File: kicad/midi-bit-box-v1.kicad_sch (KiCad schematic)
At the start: 60 parts, among them IC1 LM386, IC2 DIP14, K1 TQ2-L-5V, Q1 2N3904, Q2 2N3906, Q3 2N3904, Q4 2N3904, U1 AY-3-8910, U2 L78L09_TO92, U3 NE555P

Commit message: added trimpot to control output volume
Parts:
- added LEVEL1: 100k, midi-bit-box-v1:TRIM1, symbol midi-bit-box-v1-eagle-import:TRIMMER
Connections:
- net GND: now also LEVEL1.1
- net at OUTPUT1.T: now also LEVEL1.2; no longer K1.8
- new net: K1.8, LEVEL1.3
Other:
- moved on the sheet: OUTPUT1
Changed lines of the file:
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@@
+    (stroke (width 0) (type default) (color 0 0 0 0))
+  )
+  (wire (pts (xy 373.126 162.052) (xy 373.126 165.862))
     (stroke (width 0) (type default) (color 0 0 0 0))
   )
@@
     (stroke (width 0) (type default) (color 0 0 0 0))
   )
-  (wire (pts (xy 321.31 167.64) (xy 391.668 167.64))
-    (stroke (width 0) (type default) (color 0 0 0 0))
-  )
   (wire (pts (xy 424.18 97.79) (xy 414.02 97.79))
     (stroke (width 0) (type default) (color 0 0 0 0))
   )
+  (wire (pts (xy 321.31 167.64) (xy 345.948 167.64))
+    (stroke (width 0) (type default) (color 0 0 0 0))
+  )
   (wire (pts (xy 121.92 55.88) (xy 121.92 76.2))
     (stroke (width 0) (type default) (color 0 0 0 0))
@@
     (stroke (width 0) (type default) (color 0 0 0 0))
   )
+  (wire (pts (xy 345.948 162.052) (xy 356.362 162.052))
+    (stroke (width 0) (type default) (color 0 0 0 0))
+  )
   (wire (pts (xy 331.978 242.316) (xy 344.678 242.316))
     (stroke (width 0) (type default) (color 0 0 0 0))
@@
     (stroke (width 0) (type default) (color 0 0 0 0))
   )
+  (wire (pts (xy 385.826 157.734) (xy 385.826 159.766))
+    (stroke (width 0) (type default) (color 0 0 0 0))
+  )
   (wire (pts (xy 162.56 25.4) (xy 162.56 27.94))
     (stroke (width 0) (type default) (color 0 0 0 0))
@@
     (stroke (width 0) (type default) (color 0 0 0 0))
   )
-  (wire (pts (xy 391.668 164.846) (xy 391.668 167.64))
-    (stroke (width 0) (type default) (color 0 0 0 0))
-  )
   (wire (pts (xy 240.03 17.78) (xy 224.79 17.78))
     (stroke (width 0) (type default) (color 0 0 0 0))
@@
     (stroke (width 0) (type default) (color 0 0 0 0))
   )
-  (wire (pts (xy 397.51 162.306) (xy 386.08 162.306))
+  (wire (pts (xy 396.748 155.194) (xy 385.318 155.194))
     (stroke (width 0) (type default) (color 0 0 0 0))
   )
@@
     (stroke (width 0) (type default) (color 0 0 0 0))
   )
+  (wire (pts (xy 396.748 157.734) (xy 385.826 157.734))
+    (stroke (width 0) (type default) (color 0 0 0 0))
+  )
   (wire (pts (xy 294.64 172.72) (xy 294.64 187.96))
     (stroke (width 0) (type default) (color 0 0 0 0))
@@
     (stroke (width 0) (type default) (color 0 0 0 0))
   )
+  (wire (pts (xy 369.062 162.052) (xy 373.126 162.052))
+    (stroke (width 0) (type default) (color 0 0 0 0))
+  )
   (wire (pts (xy 212.09 81.28) (xy 220.98 81.28))
     (stroke (width 0) (type default) (color 0 0 0 0))
@@
     (stroke (width 0) (type default) (color 0 0 0 0))
   )
+  (wire (pts (xy 371.348 159.766) (xy 371.348 153.416))
+    (stroke (width 0) (type default) (color 0 0 0 0))
+  )
   (wire (pts (xy 57.15 50.8) (xy 68.58 50.8))
     (stroke (width 0) (type default) (color 0 0 0 0))
@@
     (stroke (width 0) (type default) (color 0 0 0 0))
   )
+  (wire (pts (xy 373.126 165.862) (xy 378.206 165.862))
+    (stroke (width 0) (type default) (color 0 0 0 0))
+  )
   (wire (pts (xy 441.96 115.57) (xy 441.96 109.22))
     (stroke (width 0) (type default) (color 0 0 0 0))
   )
-  (wire (pts (xy 397.51 164.846) (xy 391.668 164.846))
-    (stroke (width 0) (type default) (color 0 0 0 0))
-  )
   (wire (pts (xy 196.85 149.86) (xy 172.72 149.86))
     (stroke (width 0) (type default) (color 0 0 0 0))
@@
     (stroke (width 0) (type default) (color 0 0 0 0))
   )
+  (wire (pts (xy 378.206 165.862) (xy 378.206 168.656))
+    (stroke (width 0) (type default) (color 0 0 0 0))
+  )
   (wire (pts (xy 281.94 182.88) (xy 281.94 187.96))
     (stroke (width 0) (type default) (color 0 0 0 0))
@@
     (stroke (width 0) (type default) (color 0 0 0 0))
   )
+  (wire (pts (xy 385.826 159.766) (xy 371.348 159.766))
+    (stroke (width 0) (type default) (color 0 0 0 0))
+  )
   (wire (pts (xy 434.34 97.79) (xy 441.96 97.79))
     (stroke (width 0) (type default) (color 0 0 0 0))
@@
     (stroke (width 0) (type default) (color 0 0 0 0))
   )
+  (wire (pts (xy 362.712 153.416) (xy 362.712 156.972))
+    (stroke (width 0) (type default) (color 0 0 0 0))
+  )
   (wire (pts (xy 375.666 239.776) (xy 382.778 239.776))
     (stroke (width 0) (type default) (color 0 0 0 0))
@@
     (stroke (width 0) (type default) (color 0 0 0 0))
   )
+  (wire (pts (xy 345.948 167.64) (xy 345.948 162.052))
+    (stroke (width 0) (type default) (color 0 0 0 0))
+  )
   (wire (pts (xy 132.08 93.98) (xy 144.78 93.98))
     (stroke (width 0) (type default) (color 0 0 0 0))
@@
   )
   (wire (pts (xy 396.24 13.97) (xy 388.62 13.97))
+    (stroke (width 0) (type default) (color 0 0 0 0))
+  )
+  (wire (pts (xy 371.348 153.416) (xy 362.712 153.416))
     (stroke (width 0) (type default) (color 0 0 0 0))
   )
@@
     (pin "1")
   )
-  (symbol (lib_id "Connector:AudioJack2") (at 402.59 164.846 0) (mirror y) (unit 1)
+  (symbol (lib_id "Connector:AudioJack2") (at 401.828 157.734 0) (mirror y) (unit 1)
     (in_bom yes) (on_board yes) (fields_autoplaced)
-    (property "Reference" "OUTPUT1" (id 0) (at 407.67 162.9409 0)
+    (property "Reference" "OUTPUT1" (id 0) (at 406.908 155.8289 0)
       (effects (font (size 1.27 1.27)) (justify right))
     )
-    (property "Value" "Audio Jack" (id 1) (at 407.67 165.4809 0)
+    (property "Value" "Audio Jack" (id 1) (at 406.908 158.3689 0)
       (effects (font (size 1.27 1.27)) (justify right))
     )
-    (property "Footprint" "midi-bit-box-v1:2PADS" (id 2) (at 402.59 164.846 0)
-      (effects (font (size 1.27 1.27)) hide)
-    )
-    (property "Datasheet" "~" (id 3) (at 402.59 164.846 0)
+    (property "Footprint" "midi-bit-box-v1:2PADS" (id 2) (at 401.828 157.734 0)
+      (effects (font (size 1.27 1.27)) hide)
+    )
+    (property "Datasheet" "~" (id 3) (at 401.828 157.734 0)
       (effects (font (size 1.27 1.27)) hide)
     )
@@
     (property "Datasheet" "https://www.onsemi.com/pub/Collateral/2N3903-D.PDF" (id 3) (at 365.76 187.96 0)
       (effects (font (size 1.27 1.27)) (justify left) hide)
+    )
+    (pin "1")
+    (pin "2")
+    (pin "3")
+  )
+  (symbol (lib_id "midi-bit-box-v1-eagle-import:TRIMMER") (at 362.712 162.052 90) (unit 1)
+    (in_bom yes) (on_board yes)
+    (property "Reference" "LEVEL1" (id 0) (at 362.712 164.211 90)
+      (effects (font (size 1.778 1.5113)))
+    )
+    (property "Value" "100k" (id 1) (at 362.712 166.497 90)
+      (effects (font (size 1.778 1.5113)))
+    )
+    (property "Footprint" "midi-bit-box-v1:TRIM1" (id 2) (at 362.712 162.052 0)
+      (effects (font (size 1.27 1.27)) hide)
+    )
+    (property "Datasheet" "" (id 3) (at 362.712 162.052 0)
+      (effects (font (size 1.27 1.27)) hide)
     )
     (pin "1")
@@
     (pin "2")
   )
-  (symbol (lib_id "midi-bit-box-v1-eagle-import:GND") (at 383.54 162.306 270) (unit 1)
-    (in_bom yes) (on_board yes)
-    (property "Reference" "#GND028" (id 0) (at 383.54 162.306 0)
-      (effects (font (size 1.27 1.27)) hide)
-    )
-    (property "Value" "GND" (id 1) (at 380.365 160.401 0)
-      (effects (font (size 1.778 1.5113)) (justify left bottom))
-    )
-    (property "Footprint" "midi-bit-box-v1:" (id 2) (at 383.54 162.306 0)
-      (effects (font (size 1.27 1.27)) hide)
-    )
-    (property "Datasheet" "" (id 3) (at 383.54 162.306 0)
+  (symbol (lib_id "midi-bit-box-v1-eagle-import:GND") (at 382.778 155.194 270) (unit 1)
+    (in_bom yes) (on_board yes)
+    (property "Reference" "#GND028" (id 0) (at 382.778 155.194 0)
+      (effects (font (size 1.27 1.27)) hide)
+    )
+    (property "Value" "GND" (id 1) (at 379.603 153.289 0)
+      (effects (font (size 1.778 1.5113)) (justify left bottom))
+    )
+    (property "Footprint" "midi-bit-box-v1:" (id 2) (at 382.778 155.194 0)
+      (effects (font (size 1.27 1.27)) hide)
+    )
+    (property "Datasheet" "" (id 3) (at 382.778 155.194 0)
       (effects (font (size 1.27 1.27)) hide)
     )
@@
     )
     (property "Datasheet" "" (id 3) (at 397.51 267.97 0)
+      (effects (font (size 1.27 1.27)) hide)
+    )
+    (pin "1")
+  )
+  (symbol (lib_id "midi-bit-box-v1-eagle-import:GND") (at 378.206 171.196 0) (unit 1)
+    (in_bom yes) (on_board yes)
+    (property "Reference" "#GND017" (id 0) (at 378.206 171.196 0)
+      (effects (font (size 1.27 1.27)) hide)
+    )
+    (property "Value" "GND" (id 1) (at 376.301 174.371 0)
+      (effects (font (size 1.778 1.5113)) (justify left bottom))
+    )
+    (property "Footprint" "midi-bit-box-v1:" (id 2) (at 378.206 171.196 0)
+      (effects (font (size 1.27 1.27)) hide)
+    )
+    (property "Datasheet" "" (id 3) (at 378.206 171.196 0)
       (effects (font (size 1.27 1.27)) hide)
     )
@@
       (reference "#GND016") (unit 1) (value "GND") (footprint "midi-bit-box-v1:")
     )
+    (path "/b95cf37c-654d-489a-853a-72e5854049e9"
+      (reference "#GND017") (unit 1) (value "GND") (footprint "midi-bit-box-v1:")
+    )
     (path "/bfff8af5-be9c-44df-80bd-23ee2cf9c437"
       (reference "#GND018") (unit 1) (value "GND") (footprint "midi-bit-box-v1:")
@@
       (reference "K1") (unit 1) (value "TQ2-L-5V") (footprint "TQ2-L-5V:Panasonic-TQ2-L-5V-MFG")
     )
+    (path "/5f2ba9a3-b109-4cb2-9e98-0eb18a1c208a"
+      (reference "LEVEL1") (unit 1) (value "100k") (footprint "midi-bit-box-v1:TRIM1")
+    )
     (path "/7a332b0c-4cba-438b-85c1-9efe2690fb62"

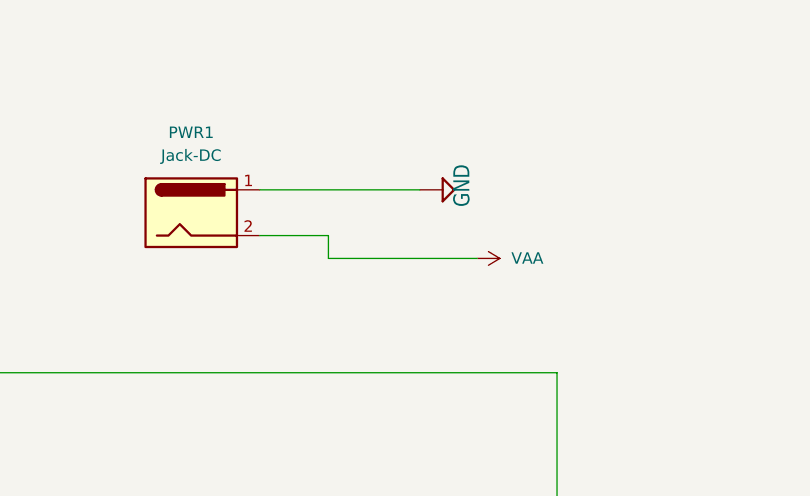
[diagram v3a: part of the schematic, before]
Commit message: corrected DC input jack pads
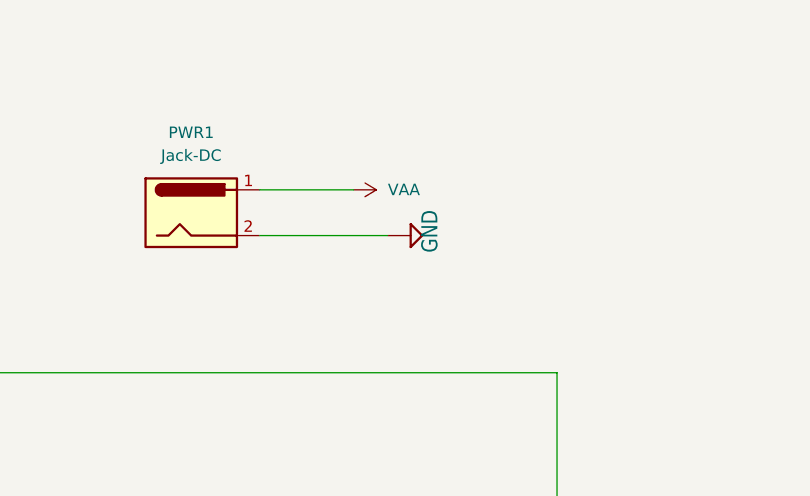
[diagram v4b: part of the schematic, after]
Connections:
- net GND: now also PWR1.2; no longer PWR1.1
- net VAA: now also PWR1.1; no longer PWR1.2
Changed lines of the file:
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@@
-    (stroke (width 0) (type default) (color 0 0 0 0))
-  )
-  (wire (pts (xy 162.56 25.4) (xy 162.56 27.94))
     (stroke (width 0) (type default) (color 0 0 0 0))
   )
@@
     (stroke (width 0) (type default) (color 0 0 0 0))
   )
+  (wire (pts (xy 154.94 25.4) (xy 169.164 25.4))
+    (stroke (width 0) (type default) (color 0 0 0 0))
+  )
   (wire (pts (xy 429.26 34.29) (xy 414.02 34.29))
     (stroke (width 0) (type default) (color 0 0 0 0))
@@
     (stroke (width 0) (type default) (color 0 0 0 0))
   )
+  (wire (pts (xy 154.94 20.32) (xy 165.354 20.32))
+    (stroke (width 0) (type default) (color 0 0 0 0))
+  )
   (wire (pts (xy 576.58 113.03) (xy 576.58 69.85))
     (stroke (width 0) (type default) (color 0 0 0 0))
@@
     (stroke (width 0) (type default) (color 0 0 0 0))
   )
-  (wire (pts (xy 154.94 25.4) (xy 162.56 25.4))
-    (stroke (width 0) (type default) (color 0 0 0 0))
-  )
   (wire (pts (xy 525.78 119.38) (xy 525.78 123.19))
     (stroke (width 0) (type default) (color 0 0 0 0))
@@
     (stroke (width 0) (type default) (color 0 0 0 0))
   )
-  (wire (pts (xy 154.94 20.32) (xy 172.72 20.32))
-    (stroke (width 0) (type default) (color 0 0 0 0))
-  )
   (wire (pts (xy 497.84 97.79) (xy 515.62 97.79))
     (stroke (width 0) (type default) (color 0 0 0 0))
@@
   )
   (wire (pts (xy 241.3 193.04) (xy 241.3 187.96))
-    (stroke (width 0) (type default) (color 0 0 0 0))
-  )
-  (wire (pts (xy 162.56 27.94) (xy 179.07 27.94))
     (stroke (width 0) (type default) (color 0 0 0 0))
   )
@@
     (pin "2")
   )
-  (symbol (lib_id "power:VAA") (at 179.07 27.94 270) (unit 1)
+  (symbol (lib_id "power:VAA") (at 165.354 20.32 270) (unit 1)
     (in_bom yes) (on_board yes) (fields_autoplaced)
-    (property "Reference" "#PWR02" (id 0) (at 175.26 27.94 0)
-      (effects (font (size 1.27 1.27)) hide)
-    )
-    (property "Value" "VAA" (id 1) (at 182.88 27.9399 90)
+    (property "Reference" "#PWR02" (id 0) (at 161.544 20.32 0)
+      (effects (font (size 1.27 1.27)) hide)
+    )
+    (property "Value" "VAA" (id 1) (at 169.164 20.3199 90)
       (effects (font (size 1.27 1.27)) (justify left))
     )
-    (property "Footprint" "" (id 2) (at 179.07 27.94 0)
-      (effects (font (size 1.27 1.27)) hide)
-    )
-    (property "Datasheet" "" (id 3) (at 179.07 27.94 0)
-      (effects (font (size 1.27 1.27)) hide)
-    )
-    (pin "1")
-  )
-  (symbol (lib_name "GND_1") (lib_id "midi-bit-box-v1-eagle-import:GND") (at 175.26 20.32 90) (unit 1)
-    (in_bom yes) (on_board yes)
-    (property "Reference" "#GND04" (id 0) (at 175.26 20.32 0)
-      (effects (font (size 1.27 1.27)) hide)
-    )
-    (property "Value" "GND" (id 1) (at 178.435 22.225 0)
+    (property "Footprint" "" (id 2) (at 165.354 20.32 0)
+      (effects (font (size 1.27 1.27)) hide)
+    )
+    (property "Datasheet" "" (id 3) (at 165.354 20.32 0)
+      (effects (font (size 1.27 1.27)) hide)
+    )
+    (pin "1")
+  )
+  (symbol (lib_name "GND_1") (lib_id "midi-bit-box-v1-eagle-import:GND") (at 171.704 25.4 90) (unit 1)
+    (in_bom yes) (on_board yes)
+    (property "Reference" "#GND04" (id 0) (at 171.704 25.4 0)
+      (effects (font (size 1.27 1.27)) hide)
+    )
+    (property "Value" "GND" (id 1) (at 174.879 27.305 0)
       (effects (font (size 1.778 1.5113)) (justify left bottom))
     )
-    (property "Footprint" "midi-bit-box-v1:" (id 2) (at 175.26 20.32 0)
-      (effects (font (size 1.27 1.27)) hide)
-    )
-    (property "Datasheet" "" (id 3) (at 175.26 20.32 0)
-      (effects (font (size 1.27 1.27)) hide)
-    )
+    (property "Footprint" "midi-bit-box-v1:" (id 2) (at 171.704 25.4 0)
+      (effects (font (size 1.27 1.27)) hide)
+    )
+    (property "Datasheet" "" (id 3) (at 171.704 25.4 0)
+      (effects (font (size 1.27 1.27)) hide)
+    )
